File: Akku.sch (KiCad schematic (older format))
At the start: 47 parts, among them P1 CONN_02X10, P2 CONN_02X10, P3 CONN_02X10, SW1 SWITCH_INV, SW2 SWITCH_INV, SW3 SWITCH_INV, U1 7400, U2 7400, U3 4069, U4 74LS193, U5 74LS541, U6 74LS193, U7 74LS540

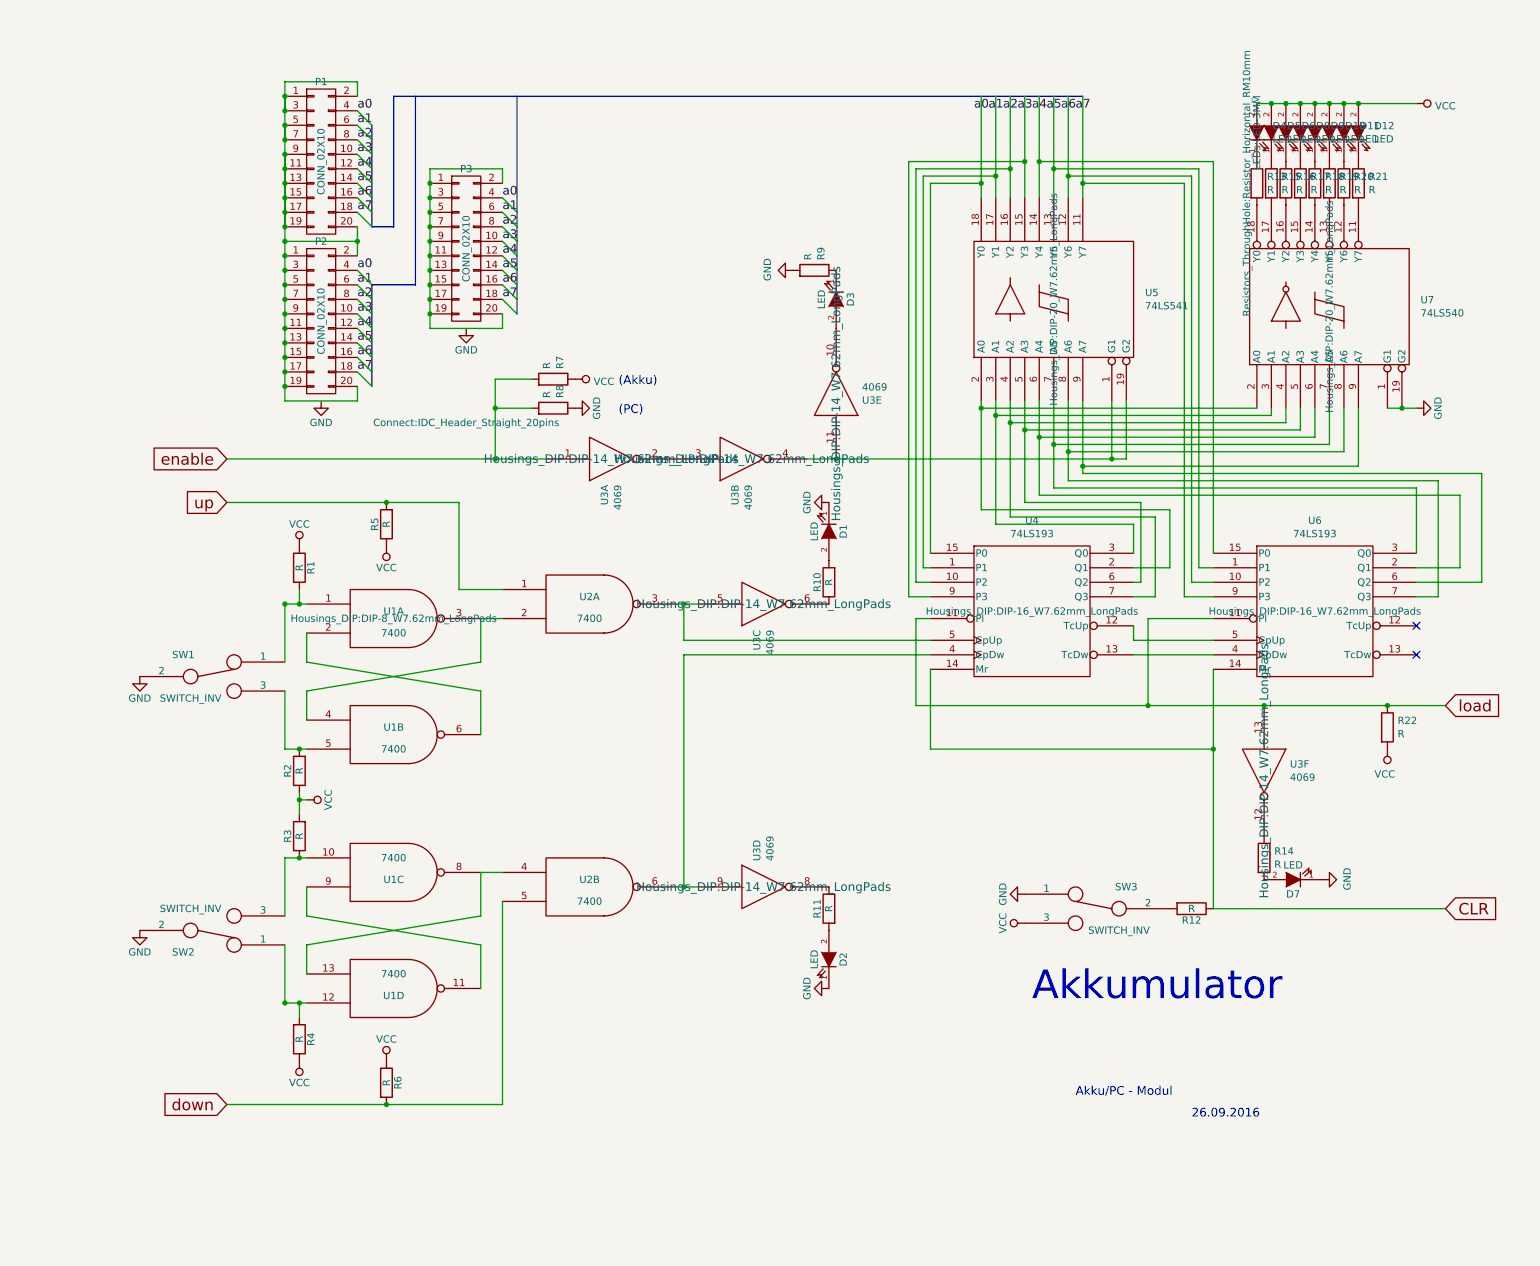
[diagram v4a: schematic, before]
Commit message: Akku Schaltplan fast fertiggestellt; PCB angefangen.
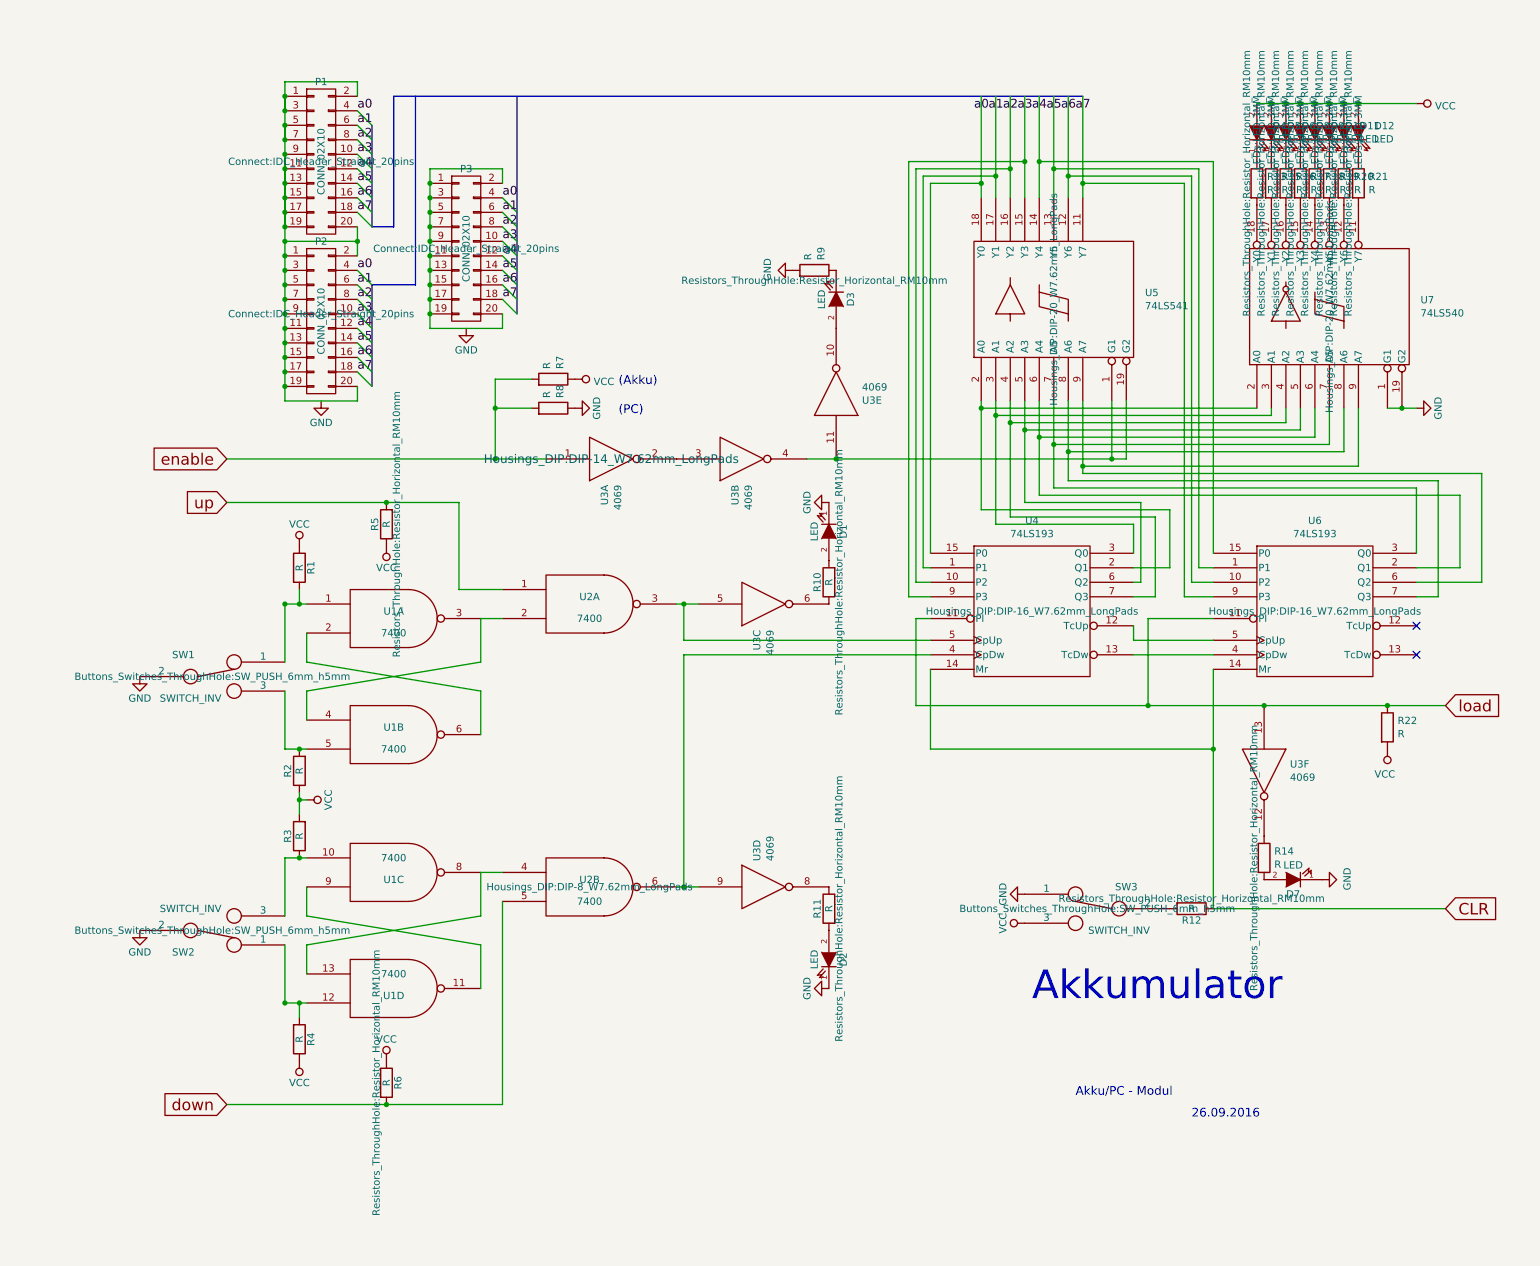
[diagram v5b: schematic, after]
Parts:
- D10, D11, D12, D5, D6, D8, D9: footprint (none) -> LEDs:LED-3MM
- P1, P2: footprint (none) -> Connect:IDC_Header_Straight_20pins
- R10, R11, R12, R14, R15, R16, R17, R18, R19, R20, R21, R5, R6, R9: footprint (none) -> Resistors_ThroughHole:Resistor_Horizontal_RM10mm
- SW1, SW2, SW3: footprint (none) -> Buttons_Switches_ThroughHole:SW_PUSH_6mm_h5mm
- U1: footprint Housings_DIP:DIP-8_W7.62mm_LongPads -> (none)
- U2: footprint (none) -> Housings_DIP:DIP-8_W7.62mm_LongPads
- U3: footprint Housings_DIP:DIP-14_W7.62mm_LongPads -> (none)
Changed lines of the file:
@@
 F 0 "D12" V 9346 742 50  0000 R CNN
 F 1 "LED" V 9255 742 50  0000 R CNN
-F 2 "" H 9300 850 50  0000 C CNN
+F 2 "LEDs:LED-3MM" H 9300 850 50  0000 C CNN
 F 3 "" H 9300 850 50  0000 C CNN
 	1    9300 850
@@
 F 0 "D11" V 9246 742 50  0000 R CNN
 F 1 "LED" V 9155 742 50  0000 R CNN
-F 2 "" H 9200 850 50  0000 C CNN
+F 2 "LEDs:LED-3MM" H 9200 850 50  0000 C CNN
 F 3 "" H 9200 850 50  0000 C CNN
 	1    9200 850
@@
 F 0 "D10" V 9146 742 50  0000 R CNN
 F 1 "LED" V 9055 742 50  0000 R CNN
-F 2 "" H 9100 850 50  0000 C CNN
+F 2 "LEDs:LED-3MM" H 9100 850 50  0000 C CNN
 F 3 "" H 9100 850 50  0000 C CNN
 	1    9100 850
@@
 F 0 "D9" V 9046 742 50  0000 R CNN
 F 1 "LED" V 8955 742 50  0000 R CNN
-F 2 "" H 9000 850 50  0000 C CNN
+F 2 "LEDs:LED-3MM" H 9000 850 50  0000 C CNN
 F 3 "" H 9000 850 50  0000 C CNN
 	1    9000 850
@@
 F 0 "D8" V 8946 742 50  0000 R CNN
 F 1 "LED" V 8855 742 50  0000 R CNN
-F 2 "" H 8900 850 50  0000 C CNN
+F 2 "LEDs:LED-3MM" H 8900 850 50  0000 C CNN
 F 3 "" H 8900 850 50  0000 C CNN
 	1    8900 850
@@
 F 0 "D6" V 8846 742 50  0000 R CNN
 F 1 "LED" V 8755 742 50  0000 R CNN
-F 2 "" H 8800 850 50  0000 C CNN
+F 2 "LEDs:LED-3MM" H 8800 850 50  0000 C CNN
 F 3 "" H 8800 850 50  0000 C CNN
 	1    8800 850
@@
 F 0 "D5" V 8746 742 50  0000 R CNN
 F 1 "LED" V 8655 742 50  0000 R CNN
-F 2 "" H 8700 850 50  0000 C CNN
+F 2 "LEDs:LED-3MM" H 8700 850 50  0000 C CNN
 F 3 "" H 8700 850 50  0000 C CNN
 	1    8700 850
@@
 F 0 "R15" H 8770 1246 50  0000 L CNN
 F 1 "R" H 8770 1155 50  0000 L CNN
-F 2 "" V 8630 1200 50  0000 C CNN
+F 2 "Resistors_ThroughHole:Resistor_Horizontal_RM10mm" V 8630 1200 50  0000 C CNN
 F 3 "" H 8700 1200 50  0000 C CNN
 	1    8700 1200
@@
 F 0 "R16" H 8870 1246 50  0000 L CNN
 F 1 "R" H 8870 1155 50  0000 L CNN
-F 2 "" V 8730 1200 50  0000 C CNN
+F 2 "Resistors_ThroughHole:Resistor_Horizontal_RM10mm" V 8730 1200 50  0000 C CNN
 F 3 "" H 8800 1200 50  0000 C CNN
 	1    8800 1200
@@
 F 0 "R17" H 8970 1246 50  0000 L CNN
 F 1 "R" H 8970 1155 50  0000 L CNN
-F 2 "" V 8830 1200 50  0000 C CNN
+F 2 "Resistors_ThroughHole:Resistor_Horizontal_RM10mm" V 8830 1200 50  0000 C CNN
 F 3 "" H 8900 1200 50  0000 C CNN
 	1    8900 1200
@@
 F 0 "R18" H 9070 1246 50  0000 L CNN
 F 1 "R" H 9070 1155 50  0000 L CNN
-F 2 "" V 8930 1200 50  0000 C CNN
+F 2 "Resistors_ThroughHole:Resistor_Horizontal_RM10mm" V 8930 1200 50  0000 C CNN
 F 3 "" H 9000 1200 50  0000 C CNN
 	1    9000 1200
@@
 F 0 "R19" H 9170 1246 50  0000 L CNN
 F 1 "R" H 9170 1155 50  0000 L CNN
-F 2 "" V 9030 1200 50  0000 C CNN
+F 2 "Resistors_ThroughHole:Resistor_Horizontal_RM10mm" V 9030 1200 50  0000 C CNN
 F 3 "" H 9100 1200 50  0000 C CNN
 	1    9100 1200
@@
 F 0 "R20" H 9270 1246 50  0000 L CNN
 F 1 "R" H 9270 1155 50  0000 L CNN
-F 2 "" V 9130 1200 50  0000 C CNN
+F 2 "Resistors_ThroughHole:Resistor_Horizontal_RM10mm" V 9130 1200 50  0000 C CNN
 F 3 "" H 9200 1200 50  0000 C CNN
 	1    9200 1200
@@
 F 0 "R21" H 9370 1246 50  0000 L CNN
 F 1 "R" H 9370 1155 50  0000 L CNN
-F 2 "" V 9230 1200 50  0000 C CNN
+F 2 "Resistors_ThroughHole:Resistor_Horizontal_RM10mm" V 9230 1200 50  0000 C CNN
 F 3 "" H 9300 1200 50  0000 C CNN
 	1    9300 1200
@@
 F 0 "U3" V 8604 5428 50  0000 L CNN
 F 1 "4069" V 8695 5428 50  0000 L CNN
-F 2 "Housings_DIP:DIP-14_W7.62mm_LongPads" H 8650 5250 60  0000 C CNN
+F 2 "" H 8650 5250 60  0000 C CNN
 F 3 "" H 8650 5250 60  0001 C CNN
 	6    8650 5250
@@
 F 0 "R14" H 8720 5896 50  0000 L CNN
 F 1 "R" H 8720 5805 50  0000 L CNN
-F 2 "" V 8580 5850 50  0000 C CNN
+F 2 "Resistors_ThroughHole:Resistor_Horizontal_RM10mm" V 8580 5850 50  0000 C CNN
 F 3 "" H 8650 5850 50  0000 C CNN
 	1    8650 5850
@@
 F 0 "U3" V 5654 2828 50  0000 L CNN
 F 1 "4069" V 5745 2828 50  0000 L CNN
-F 2 "Housings_DIP:DIP-14_W7.62mm_LongPads" H 5700 2650 60  0000 C CNN
+F 2 "" H 5700 2650 60  0000 C CNN
 F 3 "" H 5700 2650 60  0001 C CNN
 	5    5700 2650
@@
 F 0 "R9" H 5620 1846 50  0000 L CNN
 F 1 "R" H 5620 1755 50  0000 L CNN
-F 2 "" V 5480 1800 50  0000 C CNN
+F 2 "Resistors_ThroughHole:Resistor_Horizontal_RM10mm" V 5480 1800 50  0000 C CNN
 F 3 "" H 5550 1800 50  0000 C CNN
 	1    5550 1800
@@
 F 0 "R12" V 8230 6200 50  0000 C CNN
 F 1 "R" V 8150 6200 50  0000 C CNN
-F 2 "" V 8080 6200 50  0000 C CNN
+F 2 "Resistors_ThroughHole:Resistor_Horizontal_RM10mm" V 8080 6200 50  0000 C CNN
 F 3 "" H 8150 6200 50  0000 C CNN
 	1    8150 6200
@@
 F 0 "SW3" H 7300 6350 50  0000 C CNN
 F 1 "SWITCH_INV" H 7350 6050 50  0000 C CNN
-F 2 "" H 7500 6200 50  0000 C CNN
+F 2 "Buttons_Switches_ThroughHole:SW_PUSH_6mm_h5mm" H 7500 6200 50  0000 C CNN
 F 3 "" H 7500 6200 50  0000 C CNN
 	1    7500 6200
@@
 F 0 "P1" H 2150 1600 50  0000 C CNN
 F 1 "CONN_02X10" V 2150 1050 50  0000 C CNN
-F 2 "" H 2150 -150 50  0000 C CNN
+F 2 "Connect:IDC_Header_Straight_20pins" H 2150 1050 50  0000 C CNN
 F 3 "" H 2150 -150 50  0000 C CNN
 	1    2150 1050
@@
 F 0 "P2" H 2150 2700 50  0000 C CNN
 F 1 "CONN_02X10" V 2150 2150 50  0000 C CNN
-F 2 "" H 2150 950 50  0000 C CNN
+F 2 "Connect:IDC_Header_Straight_20pins" H 2150 2200 50  0000 C CNN
 F 3 "" H 2150 950 50  0000 C CNN
 	1    2150 2150
@@
 F 0 "P3" H 3150 2200 50  0000 C CNN
 F 1 "CONN_02X10" V 3150 1650 50  0000 C CNN
-F 2 "Connect:IDC_Header_Straight_20pins" H 3150 450 50  0000 C CNN
+F 2 "Connect:IDC_Header_Straight_20pins" H 3150 1650 50  0000 C CNN
 F 3 "" H 3150 450 50  0000 C CNN
 	1    3150 1650
@@
 F 0 "U3" V 5004 3278 50  0000 L CNN
 F 1 "4069" V 5095 3278 50  0000 L CNN
-F 2 "Housings_DIP:DIP-14_W7.62mm_LongPads" H 5050 3100 60  0000 C CNN
+F 2 "" H 5050 3100 60  0000 C CNN
 F 3 "" H 5050 3100 60  0001 C CNN
 	2    5050 3100
@@
 F 0 "U1" H 2650 4250 50  0000 C CNN
 F 1 "7400" H 2650 4100 50  0000 C CNN
-F 2 "Housings_DIP:DIP-8_W7.62mm_LongPads" H 2650 4200 50  0000 C CNN
+F 2 "" H 2650 4200 50  0000 C CNN
 F 3 "" H 2650 4200 50  0000 C CNN
 	1    2650 4200
@@
 F 0 "SW1" H 1200 4750 50  0000 C CNN
 F 1 "SWITCH_INV" H 1250 4450 50  0000 C CNN
-F 2 "" H 1400 4600 50  0000 C CNN
+F 2 "Buttons_Switches_ThroughHole:SW_PUSH_6mm_h5mm" H 1400 4600 50  0000 C CNN
 F 3 "" H 1400 4600 50  0000 C CNN
 	1    1400 4600
@@
 F 0 "U3" V 5154 4278 50  0000 L CNN
 F 1 "4069" V 5245 4278 50  0000 L CNN
-F 2 "Housings_DIP:DIP-14_W7.62mm_LongPads" H 5200 4100 60  0000 C CNN
+F 2 "" H 5200 4100 60  0000 C CNN
 F 3 "" H 5200 4100 60  0001 C CNN
 	3    5200 4100
@@
 F 0 "R10" V 5730 3950 50  0000 C CNN
 F 1 "R" V 5650 3950 50  0000 C CNN
-F 2 "" V 5580 3950 50  0000 C CNN
+F 2 "Resistors_ThroughHole:Resistor_Horizontal_RM10mm" V 5580 3950 50  0000 C CNN
 F 3 "" H 5650 3950 50  0000 C CNN
 	1    5650 3950
@@
 F 0 "SW2" H 1200 6500 50  0000 C CNN
 F 1 "SWITCH_INV" H 1250 6200 50  0000 C CNN
-F 2 "" H 1400 6350 50  0000 C CNN
+F 2 "Buttons_Switches_ThroughHole:SW_PUSH_6mm_h5mm" H 1400 6350 50  0000 C CNN
 F 3 "" H 1400 6350 50  0000 C CNN
 	1    1400 6350
@@
 F 0 "U3" V 5154 6228 50  0000 L CNN
 F 1 "4069" V 5245 6228 50  0000 L CNN
-F 2 "Housings_DIP:DIP-14_W7.62mm_LongPads" H 5200 6050 60  0000 C CNN
+F 2 "" H 5200 6050 60  0000 C CNN
 F 3 "" H 5200 6050 60  0001 C CNN
 	4    5200 6050
@@
 F 0 "R11" V 5730 6200 50  0000 C CNN
 F 1 "R" V 5650 6200 50  0000 C CNN
-F 2 "" V 5580 6200 50  0000 C CNN
+F 2 "Resistors_ThroughHole:Resistor_Horizontal_RM10mm" V 5580 6200 50  0000 C CNN
 F 3 "" H 5650 6200 50  0000 C CNN
 	1    5650 6200
@@
 F 0 "U2" H 4000 6100 50  0000 C CNN
 F 1 "7400" H 4000 5950 50  0000 C CNN
-F 2 "" H 4000 6050 50  0000 C CNN
+F 2 "Housings_DIP:DIP-8_W7.62mm_LongPads" H 4000 6050 50  0000 C CNN
 F 3 "" H 4000 6050 50  0000 C CNN
 	2    4000 6050
@@
 F 0 "R5" V 2680 3550 50  0000 C CNN
 F 1 "R" V 2600 3550 50  0000 C CNN
-F 2 "" V 2530 3550 50  0000 C CNN
+F 2 "Resistors_ThroughHole:Resistor_Horizontal_RM10mm" V 2530 3550 50  0000 C CNN
 F 3 "" H 2600 3550 50  0000 C CNN
 	1    2600 3550
@@
 F 0 "R6" V 2680 7400 50  0000 C CNN
 F 1 "R" V 2600 7400 50  0000 C CNN
-F 2 "" V 2530 7400 50  0000 C CNN
+F 2 "Resistors_ThroughHole:Resistor_Horizontal_RM10mm" V 2530 7400 50  0000 C CNN
 F 3 "" H 2600 7400 50  0000 C CNN
 	1    2600 7400

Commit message: Fehler am Schaltplan ausgebessert; PCB erweitert
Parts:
- U1: footprint (none) -> Housings_DIP:DIP-14_W7.62mm
- U2: value 7400 -> 7408; footprint (none) -> Housings_DIP:DIP-14_W7.62mm; symbol 7400 -> 74LS08
- U2: value 7400 -> 7408; footprint Housings_DIP:DIP-8_W7.62mm_LongPads -> Housings_DIP:DIP-14_W7.62mm; symbol 7400 -> 74LS08
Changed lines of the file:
@@
 (PC)
 $Comp
-L 7400 U2
+L 74LS08 U2
 U 1 1 580F517F
 P 4000 4100
 F 0 "U2" H 4000 4150 50  0000 C CNN
-F 1 "7400" H 4000 4000 50  0000 C CNN
-F 2 "" H 4000 4100 50  0000 C CNN
+F 1 "7408" H 4000 4000 50  0000 C CNN
+F 2 "Housings_DIP:DIP-14_W7.62mm" H 4000 4100 50  0000 C CNN
 F 3 "" H 4000 4100 50  0000 C CNN
 	1    4000 4100
@@
 F 0 "U1" H 2650 5050 50  0000 C CNN
 F 1 "7400" H 2650 4900 50  0000 C CNN
-F 2 "" H 2650 5000 50  0000 C CNN
+F 2 "Housings_DIP:DIP-14_W7.62mm" H 2650 5000 50  0000 C CNN
 F 3 "" H 2650 5000 50  0000 C CNN
 	2    2650 5000
@@
 F 0 "U1" H 2650 4250 50  0000 C CNN
 F 1 "7400" H 2650 4100 50  0000 C CNN
-F 2 "" H 2650 4200 50  0000 C CNN
+F 2 "Housings_DIP:DIP-14_W7.62mm" H 2650 4200 50  0000 C CNN
 F 3 "" H 2650 4200 50  0000 C CNN
 	1    2650 4200
@@
 F 0 "U1" H 2650 6000 50  0000 C CNN
 F 1 "7400" H 2650 5850 50  0000 C CNN
-F 2 "" H 2650 5950 50  0000 C CNN
+F 2 "Housings_DIP:DIP-14_W7.62mm" H 2650 5950 50  0000 C CNN
 F 3 "" H 2650 5950 50  0000 C CNN
 	3    2650 5950
@@
 F 0 "U1" H 2650 6800 50  0000 C CNN
 F 1 "7400" H 2650 6650 50  0000 C CNN
-F 2 "" H 2650 6750 50  0000 C CNN
+F 2 "Housings_DIP:DIP-14_W7.62mm" H 2650 6750 50  0000 C CNN
 F 3 "" H 2650 6750 50  0000 C CNN
 	4    2650 6750
@@
 $EndComp
 $Comp
-L 7400 U2
-U 2 1 581052DF
+L 74LS08 U2
+U 4 1 581052DF
 P 4000 6050
 F 0 "U2" H 4000 6100 50  0000 C CNN
-F 1 "7400" H 4000 5950 50  0000 C CNN
-F 2 "Housings_DIP:DIP-8_W7.62mm_LongPads" H 4000 6050 50  0000 C CNN
+F 1 "7408" H 4000 5950 50  0000 C CNN
+F 2 "Housings_DIP:DIP-14_W7.62mm" H 4000 6050 50  0000 C CNN
 F 3 "" H 4000 6050 50  0000 C CNN
-	2    4000 6050
-	1    0    0    -1
-$EndComp
+	4    4000 6050
+	1    0    0    -1
+$EndComp
